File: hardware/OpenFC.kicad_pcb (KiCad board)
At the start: 6 copper layers, 38.9 x 38.9 mm, 168 parts, among them CN1 SM04B-SRSS-TB, J1 5V, J10 5V, J11 5V, J12 5V, J13 5V, J14 5V, J15 5V, J16 5V, J17 5V, J18 5V, J19 5V, J2 5V, J20 5V, J21 5V, J22 5V, J23 5V, J24 5V, J25 5V, J26 5V, J27 5V, J28 5V, J29 5V, J3 5V, J30 5V, J31 5V, J32 5V, J33 5V, J34 5V, J35 5V, J36 5V, J37 5V, J38 5V, J39 5V, J4 5V, J40 5V, J41 5V, J42 5V, J43 5V, J44 5V, J47 5V, J48 5V, J49 5V, J5 5V, J50 5V, J51 5V, J52 5V, J53 5V, J54 5V, J55 5V, J6 5V, J7 5V, J8 5V, J9 5V, P1 SM08B-SRSS-TB(LF)(SN), Q1 AP1606, Q2 AP1606, U1 TS2306A 240GF MSM 9_C2976675, U10 SN74LVC1G3157DTBR, U11 COS8051SOT, U12 TLV7031DPWR, U13 SM03B-SRSS-TB, U14 SM06B-SRSS-TB(LF)(SN), U2 RP2354B_C39843328, U3 TI LMR51430YFDDCR, U4 TI LMR51430YFDDCR, U5 TPS2116DRLR, U6 NCV8187AMT180TAG, U7 LP5912-3.3DRVR, U8 SM06B-SRSS-TB(LF)(SN), U9 LSM6DSV16XTR, X1 XTM25012000JT00351001

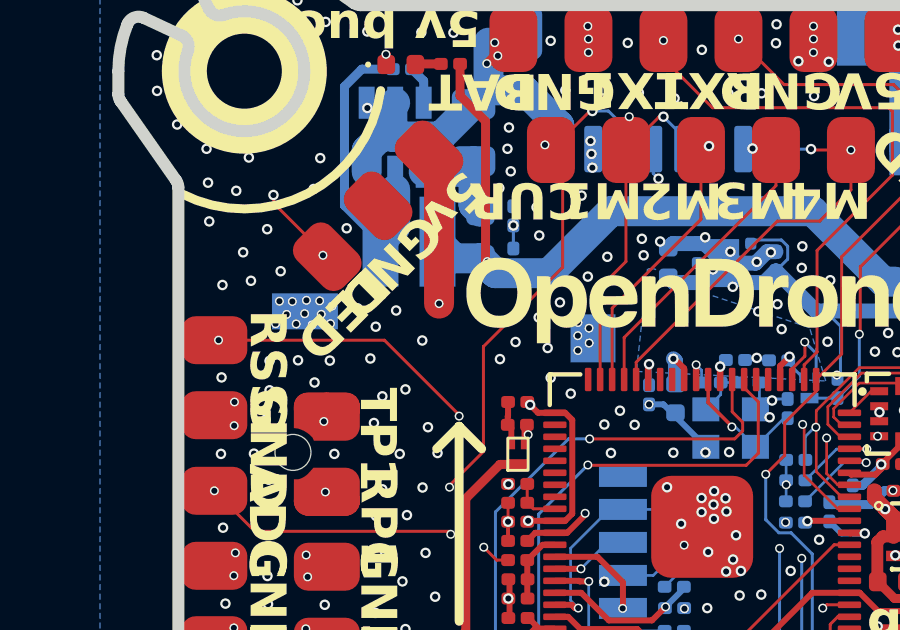
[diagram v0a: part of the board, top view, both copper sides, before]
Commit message: hardware: add LP5912-1.8 LDO (U15) and layout working state
- New LP5912-1.8DRVR symbol in project lib, WSON-6 2x2mm footprint with
  thermal vias, matching STEP model
- LP5912-1.8 added to power sheet as U15
- OpenFC.kicad_pcb layout working state carrying the change
- .kicad_pro used_designators updated (U15)

Co-Authored-By: Claude Fable 5 <noreply@anthropic.com>
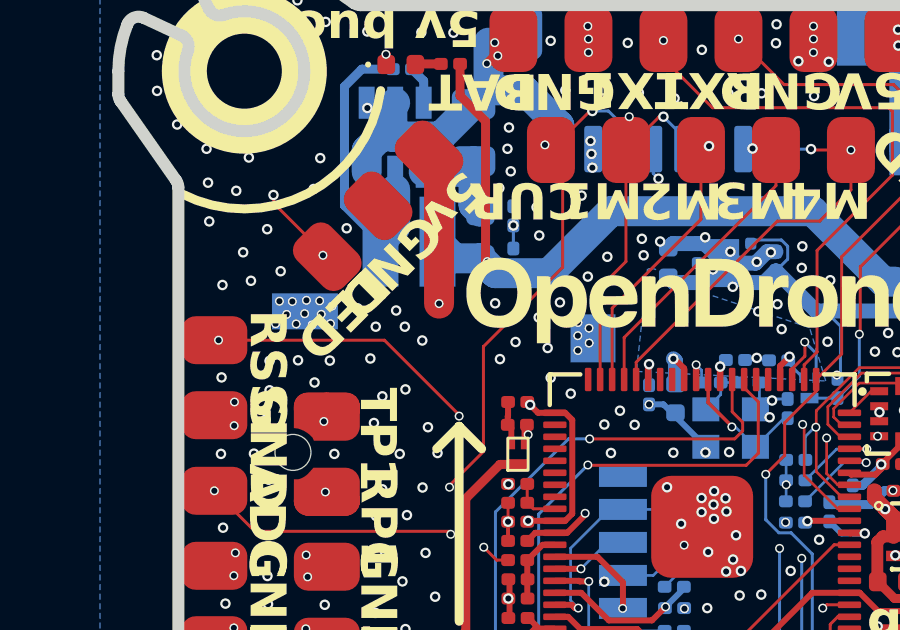
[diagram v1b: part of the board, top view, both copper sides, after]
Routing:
- net GND: vias 482 -> 484

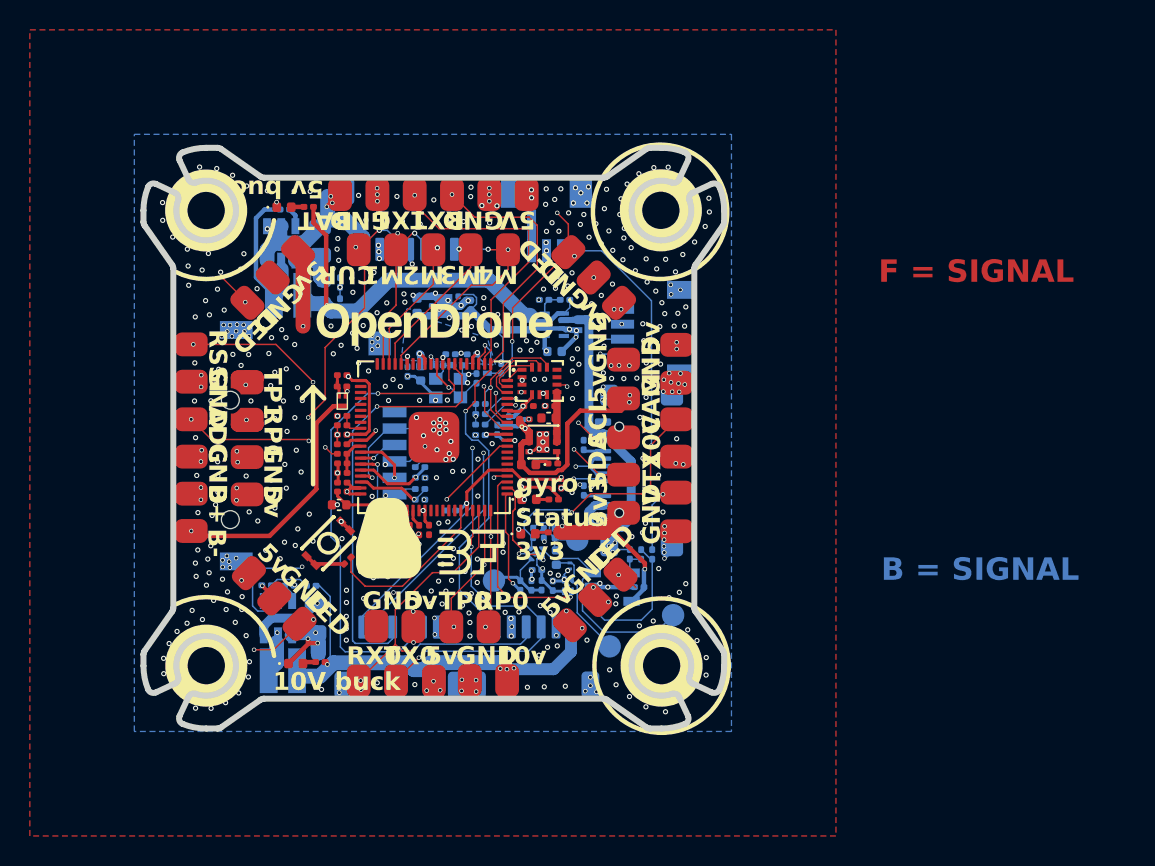
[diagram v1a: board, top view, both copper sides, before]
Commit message: Swap 1.8V LDO and IMU, fix BOM/CPL export hygiene
Mirrors the same pass done on OpenFC-Lite-Mini.

Part changes:
- NCV8187AMT180TAG (stock 0 at JLC) replaced by U15 LP5912-1.8DRVR
  (C2876234), same WSON-6 2x2 land pattern as the LP5912-3.3, PG retained.
- U9 LSM6DSV16XTR replaced by BMI270 (C2836813) in the schematic. Bosch
  Table 22 matches the existing LGA-14 symbol pin for pin, so no rewire.

Export fixes:
- U15, CN1 and U13 carried their part numbers in a field named "LCSC Part"
  rather than "LCSC" and exported blank. Renamed. CN1 (C160404) and U13
  (C160403) are real JST connectors and stay in the BOM.
- J3, J6, J10, J16, J19, J23 (lib:small_pad) and TP1 to TP4 (TestPoint) were
  still reaching the BOM with no part number. Set to in_bom=no, on_board=yes,
  dnp=no: copper stays, BOM entry goes.
- 57 pad and testpoint footprints now carry exclude_from_bom plus
  exclude_from_pos_files instead of the dnp flag. Previously 47 pads leaked
  into the position file on every export.

BOM and CPL now agree at 111 placements with no blank part numbers, exported
without any dnp flag. ERC is unchanged against HEAD (198 vs 199 violations,
all pre-existing).

Known outstanding, not in this commit: C32 is still C105226 while C42 is
C415703, and the PCB copy of U9 still carries the LSM6 part number until
Update PCB from Schematic is run. The panel file is deleted in the working
tree pending a rebuild and is deliberately left uncommitted.

Co-Authored-By: Claude Fable 5 <noreply@anthropic.com>
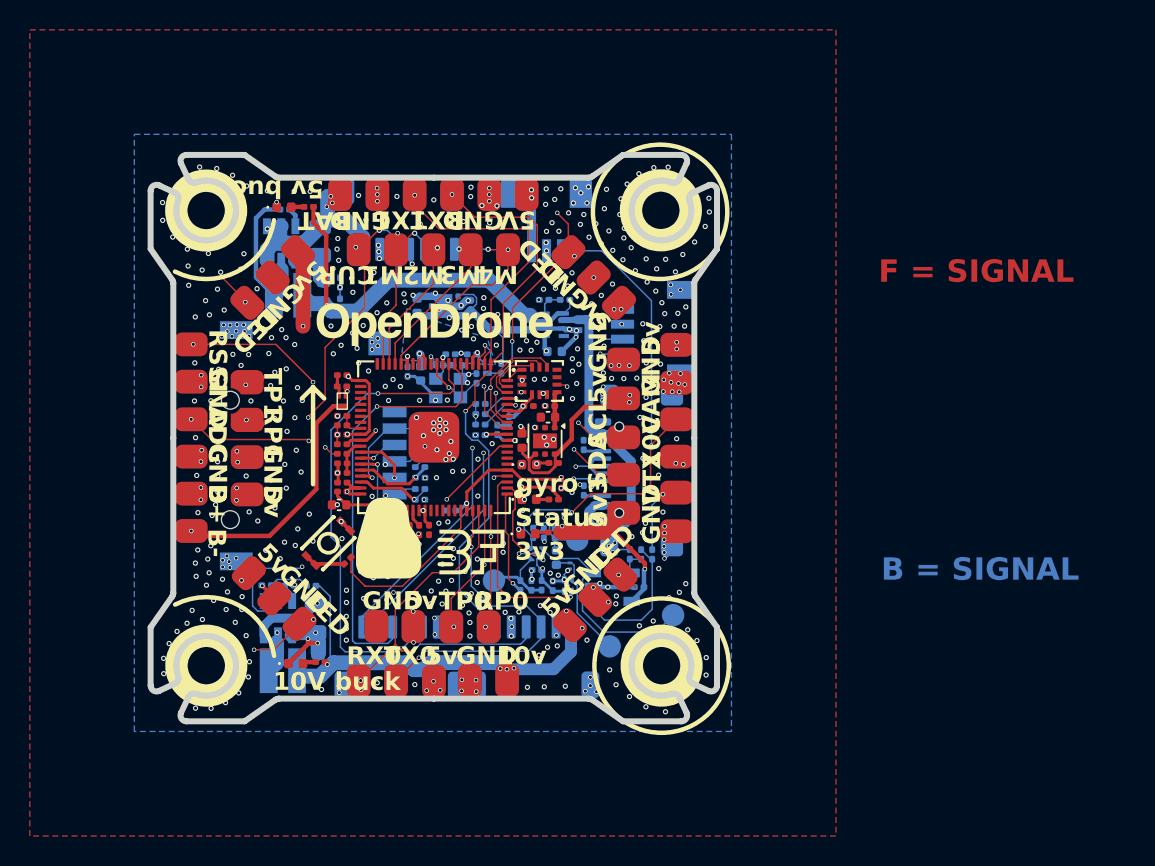
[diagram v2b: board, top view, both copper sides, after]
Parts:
- removed C29: 100n, Capacitor_SMD:C_0201_0603Metric
- removed D6: LED_1_Green, LED_SMD:LED_0402_1005Metric
- removed R27: 2.4k, Resistor_SMD:R_0201_0603Metric
- removed U6: NCV8187AMT180TAG, lib:WDFN-6_L2.0-W2.0-P0.65-BL-EP
- added C42: 22uF, Capacitor_SMD:C_0402_1005Metric, F.Cu at (160.7, 85.8)
- added D9: LED_1_Green, LED_SMD:LED_0402_1005Metric, F.Cu at (159.5, 88.9)
- added R39: 6.49k, Resistor_SMD:R_0201_0603Metric, F.Cu at (161.1, 88.8)
- added U15: LP5912-1.8DRVR, lib:WSON-6-1EP_2x2mm_P0.65mm_EP1x1.6mm_ThermalVias, F.Cu at (160.5, 87.3)
- C31: value 22uF -> 4.7uF
- moved C31 2.34 mm to (159.0, 87.3), turned to 90 degrees
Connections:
- C31 pad 1: +1.8V_GYRO -> +5V
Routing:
- net +5V: track 59.3 -> 56.4 mm, vias 28 -> 27
- net /POWER/1.8V_PG: track 0.82 -> 3.70 mm, vias 0 -> 2
- net GND: track 101.4 -> 99.3 mm, vias 484 -> 482
- net Net-(D6-K): track 0.96 -> 0.00 mm
- net +1.8V_GYRO: track 3.35 -> 2.44 mm
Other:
- board size 38.9 x 38.9 mm -> 37.9 x 37.9 mm
- board text added: "LN2 = SIGNALS"
- board text removed: "LN2 = X-SIGNALS"
